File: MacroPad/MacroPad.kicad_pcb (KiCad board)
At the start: 2 copper layers, 75 x 118 mm, 35 parts, among them SW1 CherryMX, SW10 CherryMX, SW11 CherryMX, SW12 CherryMX, SW13 RotaryEncoder_Switch, SW14 SW_Push, SW15 SW_Push, SW16 SW_Push, SW2 CherryMX, SW3 CherryMX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

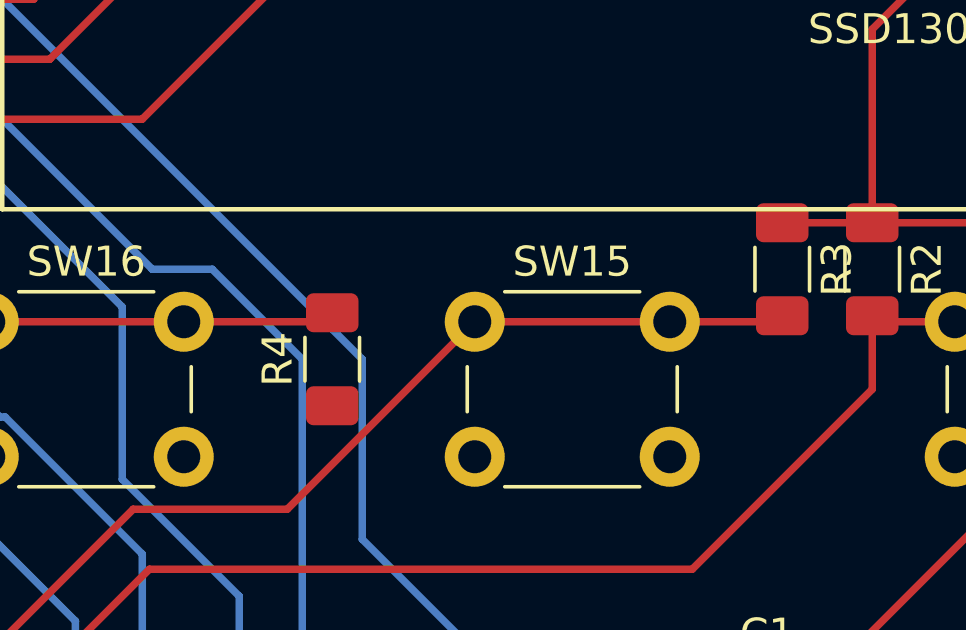
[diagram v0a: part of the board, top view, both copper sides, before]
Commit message: fixed position of R4 and GND connection
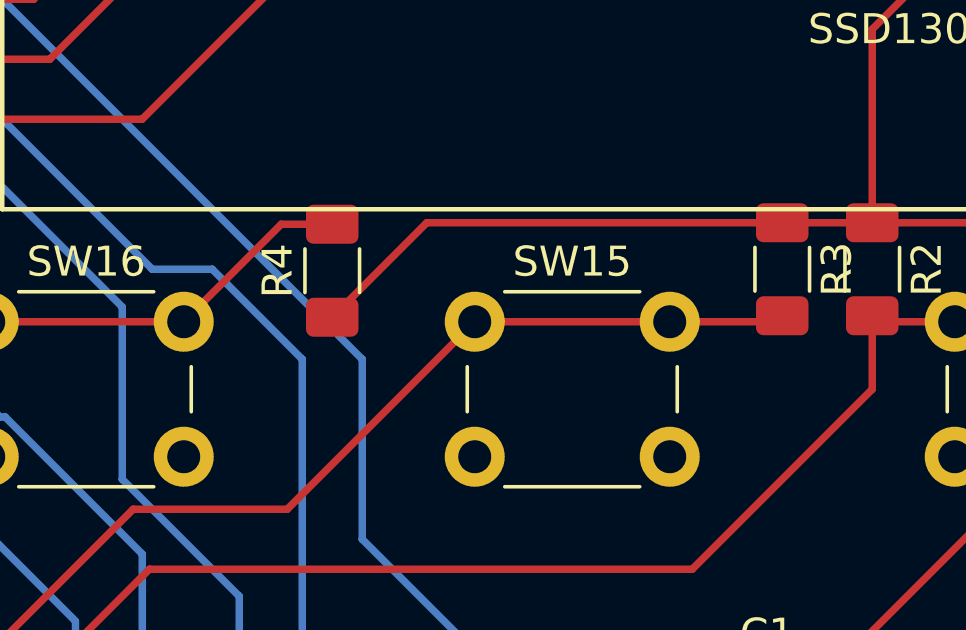
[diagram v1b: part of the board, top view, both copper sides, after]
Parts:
- moved R4 2.95 mm to (146.0, 85.0)
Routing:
- net GND: track 212.3 -> 228.6 mm
- net Button3: track 24.9 -> 26.2 mm
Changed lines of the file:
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@@
   )
   (footprint "Resistor_SMD:R_1206_3216Metric_Pad1.30x1.75mm_HandSolder" (layer "F.Cu")
-    (at 146 88 90)
+    (at 146 85.05 90)
     (descr "Resistor SMD 1206 (3216 Metric), square (rectangular) end terminal, IPC_7351 nominal with elongated pad for handsoldering. (Body size source: IPC-SM-782 page 72, https://www.pcb-3d.com/wordpress/wp-content/uploads/ipc-sm-782a_amendment_1_and_2.pdf), generated with kicad-footprint-generator")
     (tags "resistor handsolder")
@@
   (segment (start 117.55 174.4) (end 117.55 169.591919) (width 0.25) (layer "F.Cu") (net 2))
   (segment (start 146.42 165.42) (end 142.54 165.42) (width 0.25) (layer "F.Cu") (net 2))
+  (segment (start 149.15 83.45) (end 161 83.45) (width 0.25) (layer "F.Cu") (net 2))
   (segment (start 151.02 153.9) (end 142.54 145.42) (width 0.25) (layer "F.Cu") (net 2))
   (segment (start 137.55 109.591919) (end 141.721919 105.42) (width 0.25) (layer "F.Cu") (net 2))
@@
   (segment (start 162.0625 99) (end 162.54 99.4775) (width 0.25) (layer "F.Cu") (net 2))
   (segment (start 137.55 174.4) (end 137.55 169.591919) (width 0.25) (layer "F.Cu") (net 2))
+  (segment (start 146 86.6) (end 149.15 83.45) (width 0.25) (layer "F.Cu") (net 2))
   (segment (start 161 83.45) (end 164 83.45) (width 0.25) (layer "F.Cu") (net 2))
   (segment (start 137.55 129.591919) (end 141.721919 125.42) (width 0.25) (layer "F.Cu") (net 2))
@@
   (segment (start 161 86.55) (end 160.8 86.75) (width 0.25) (layer "F.Cu") (net 49))
   (segment (start 150.75 86.75) (end 157.25 86.75) (width 0.25) (layer "F.Cu") (net 49))
-  (segment (start 146 86.45) (end 145.7 86.75) (width 0.25) (layer "F.Cu") (net 50))
+  (segment (start 144.3 83.5) (end 141.05 86.75) (width 0.25) (layer "F.Cu") (net 50))
   (segment (start 134.55 86.75) (end 141.05 86.75) (width 0.25) (layer "F.Cu") (net 50))
+  (segment (start 146 83.5) (end 144.3 83.5) (width 0.25) (layer "F.Cu") (net 50))
   (segment (start 131.12344 90.17656) (end 134.55 86.75) (width 0.25) (layer "F.Cu") (net 50))
   (segment (start 131.12344 98.7) (end 131.12344 90.17656) (width 0.25) (layer "F.Cu") (net 50))
-  (segment (start 145.7 86.75) (end 141.05 86.75) (width 0.25) (layer "F.Cu") (net 50))
   (zone (net 1) (net_name "Net-(C1-Pad1)") (layer "F.Cu") (hatch edge 0.508)
     (connect_pads (clearance 0.5))

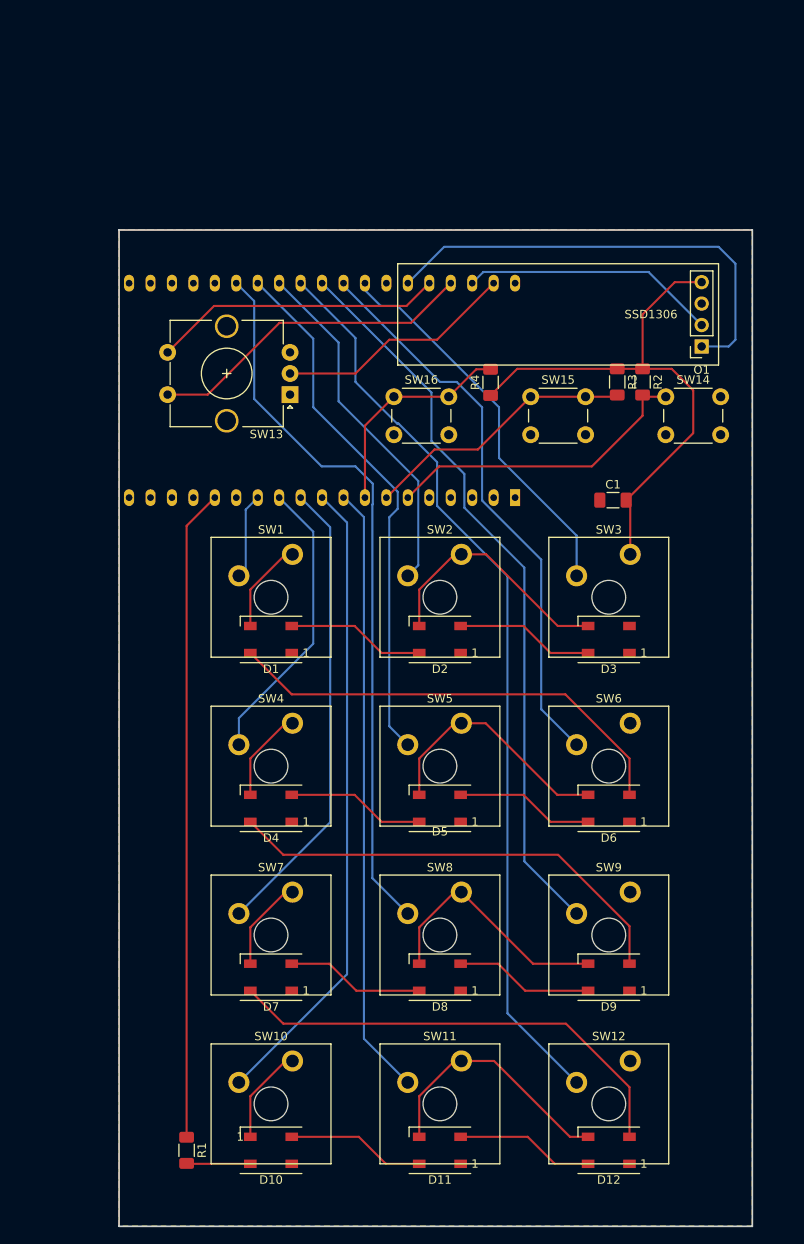
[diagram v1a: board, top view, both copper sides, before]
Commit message: updated PCB to devkitC V2
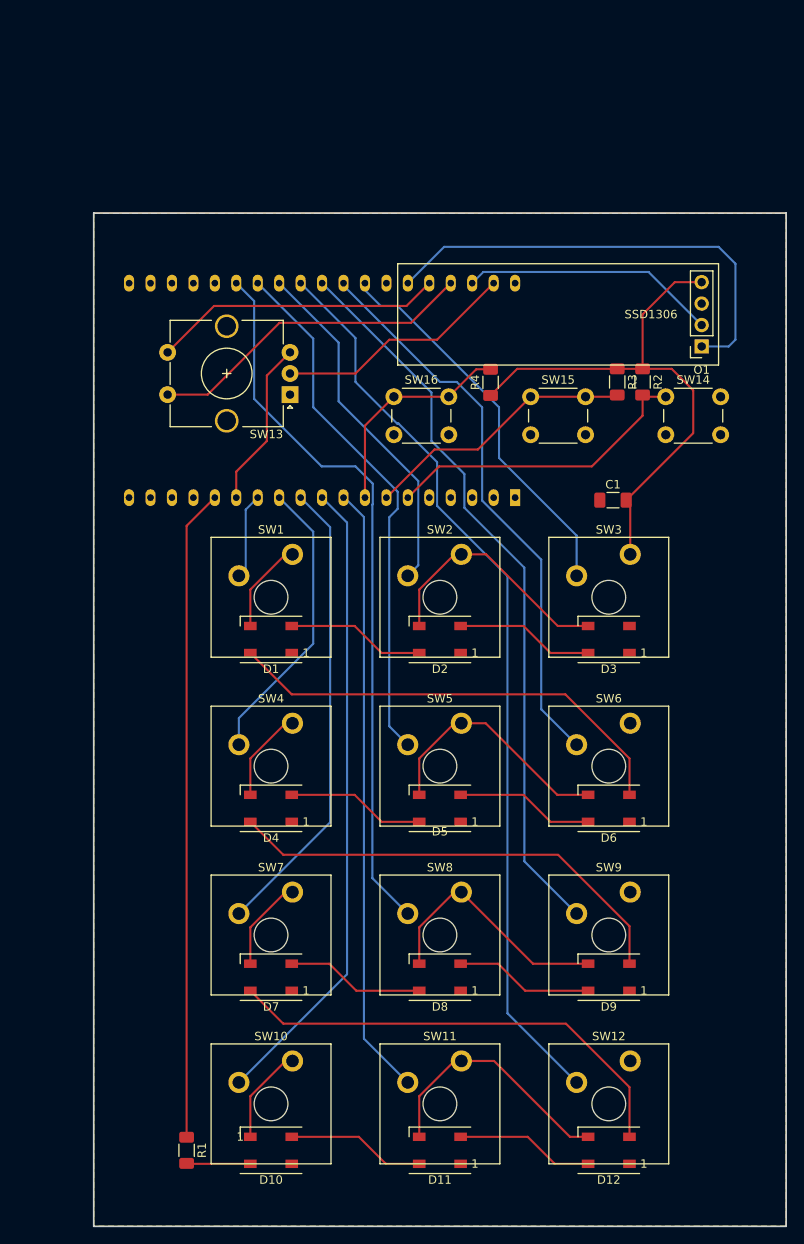
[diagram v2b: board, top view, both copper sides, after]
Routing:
- net GND: track 228.6 -> 248.5 mm
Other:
- board size 75 x 118 mm -> 82 x 120 mm
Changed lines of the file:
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@@
   (gr_line (start 135 83) (end 173 83) (layer "F.SilkS") (width 0.15))
   (gr_line (start 173 83) (end 173 71) (layer "F.SilkS") (width 0.15))
-  (gr_rect (start 102 67) (end 177 185) (layer "Edge.Cuts") (width 0.2) (fill none))
+  (gr_rect (start 99 65) (end 181 185) (layer "Edge.Cuts") (width 0.2) (fill none))
+  (segment (start 115.88344 95.61656) (end 115.88344 98.7) (width 0.25) (layer "F.Cu") (net 2))
   (segment (start 117.55 153.9) (end 117.55 149.591919) (width 0.25) (layer "F.Cu") (net 2))
   (segment (start 141.721919 105.42) (end 142.54 105.42) (width 0.25) (layer "F.Cu") (net 2))
@@
   (segment (start 155.4 174.4) (end 146.42 165.42) (width 0.25) (layer "F.Cu") (net 2))
   (segment (start 145.42 125.42) (end 142.54 125.42) (width 0.25) (layer "F.Cu") (net 2))
+  (segment (start 119.5 92) (end 115.88344 95.61656) (width 0.25) (layer "F.Cu") (net 2))
   (segment (start 117.55 174.4) (end 117.55 169.591919) (width 0.25) (layer "F.Cu") (net 2))
   (segment (start 146.42 165.42) (end 142.54 165.42) (width 0.25) (layer "F.Cu") (net 2))
@@
   (segment (start 121.721919 125.42) (end 122.54 125.42) (width 0.25) (layer "F.Cu") (net 2))
   (segment (start 117.55 133.9) (end 117.55 129.591919) (width 0.25) (layer "F.Cu") (net 2))
+  (segment (start 119.5 84.25) (end 119.5 92) (width 0.25) (layer "F.Cu") (net 2))
   (segment (start 157.55 174.4) (end 155.4 174.4) (width 0.25) (layer "F.Cu") (net 2))
   (segment (start 162.54 99.4775) (end 162.54 105.42) (width 0.25) (layer "F.Cu") (net 2))
   (segment (start 117.55 109.591919) (end 117.55 113.9) (width 0.25) (layer "F.Cu") (net 2))
+  (segment (start 122.25 81.5) (end 119.5 84.25) (width 0.25) (layer "F.Cu") (net 2))
   (segment (start 153.9 133.9) (end 145.42 125.42) (width 0.25) (layer "F.Cu") (net 2))
   (segment (start 171 73.18) (end 167.82 73.18) (width 0.25) (layer "F.Cu") (net 2))
@@
     (polygon
       (pts
-        (xy 177 185)
-        (xy 102 185)
-        (xy 102 67)
-        (xy 177 67)
+        (xy 181 185)
+        (xy 99 185)
+        (xy 99 65)
+        (xy 181 65)
       )
     )
@@
     (polygon
       (pts
-        (xy 177 185)
-        (xy 102 185)
-        (xy 102 67)
-        (xy 177 67)
+        (xy 181 185)
+        (xy 99 185)
+        (xy 99 65)
+        (xy 181 65)
       )
     )

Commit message: Plotted and Generated Drill and SVG files
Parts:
- added REF**: MountingHole_2.2mm_M2, MountingHole:MountingHole_2.2mm_M2, F.Cu at (94.0, 46.0)
- added REF**: MountingHole_2.2mm_M2, MountingHole:MountingHole_2.2mm_M2, F.Cu at (94.0, 158.0)
- added REF**: MountingHole_2.2mm_M2, MountingHole:MountingHole_2.2mm_M2, F.Cu at (168.0, 158.0)
- added REF**: MountingHole_2.2mm_M2, MountingHole:MountingHole_2.2mm_M2, F.Cu at (168.0, 46.0)
- moved SW16 24.7 mm to (125.5, 63.8)
- moved C1 24.7 mm to (151.5, 76.0)
- moved D1 24.7 mm to (111.0, 92.5)
- moved D10 24.7 mm to (111.0, 153.0)
- moved D11 24.7 mm to (131.0, 153.0)
- moved D12 24.7 mm to (151.0, 153.0)
- moved D2 24.7 mm to (131.0, 92.5)
- moved D3 24.7 mm to (151.0, 92.5)
- moved D4 24.7 mm to (111.0, 112.5)
- moved D5 24.7 mm to (131.0, 112.5)
- moved D6 24.7 mm to (151.0, 112.5)
- moved D7 24.7 mm to (111.0, 132.5)
- moved D8 24.7 mm to (131.0, 132.5)
- moved D9 24.7 mm to (151.0, 132.5)
- moved O1 24.7 mm to (162.0, 57.8)
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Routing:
- net GND: track 248.5 -> 306.1 mm
- net Net-(O1-Pad1): track 54.7 -> 53.2 mm
- net Net-(D1-Pad4): track 54.4 -> 55.5 mm
- net Net-(D4-Pad4): track 54.5 -> 55.5 mm

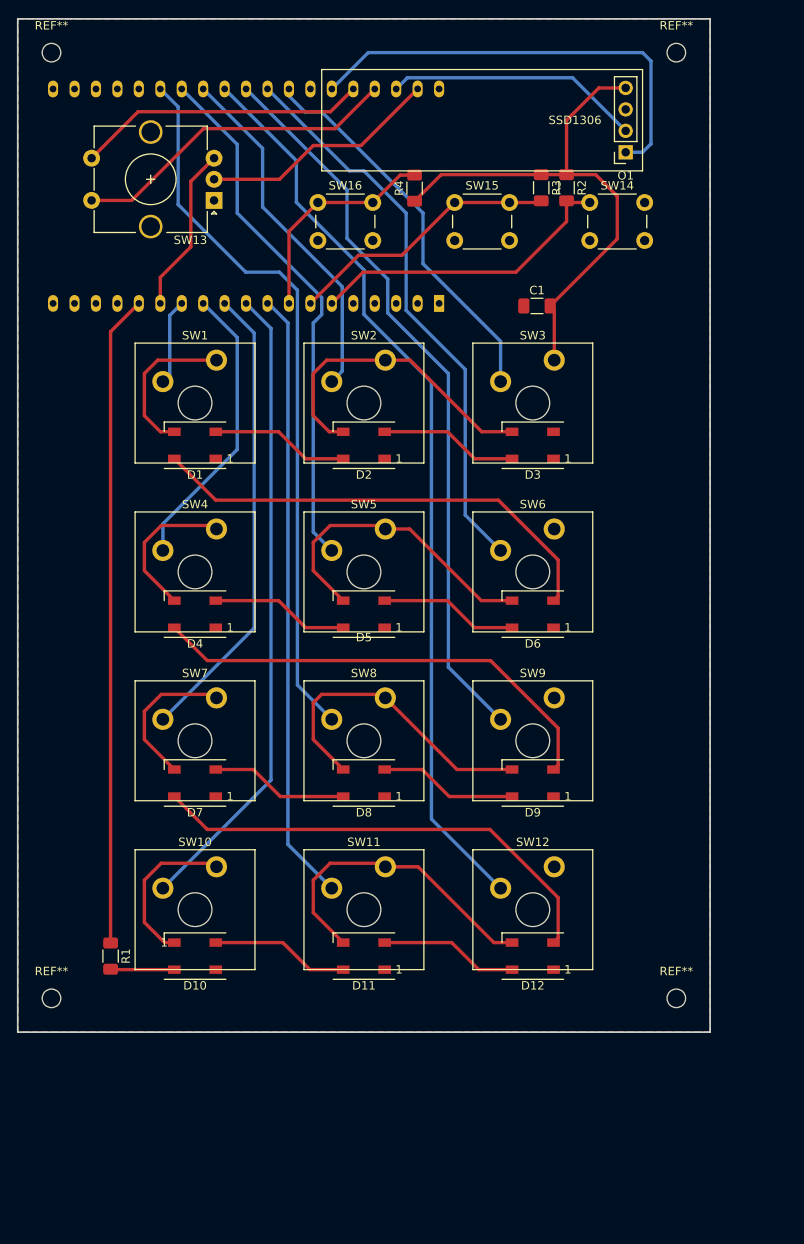
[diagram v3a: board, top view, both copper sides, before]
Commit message: Updated Silkscreen
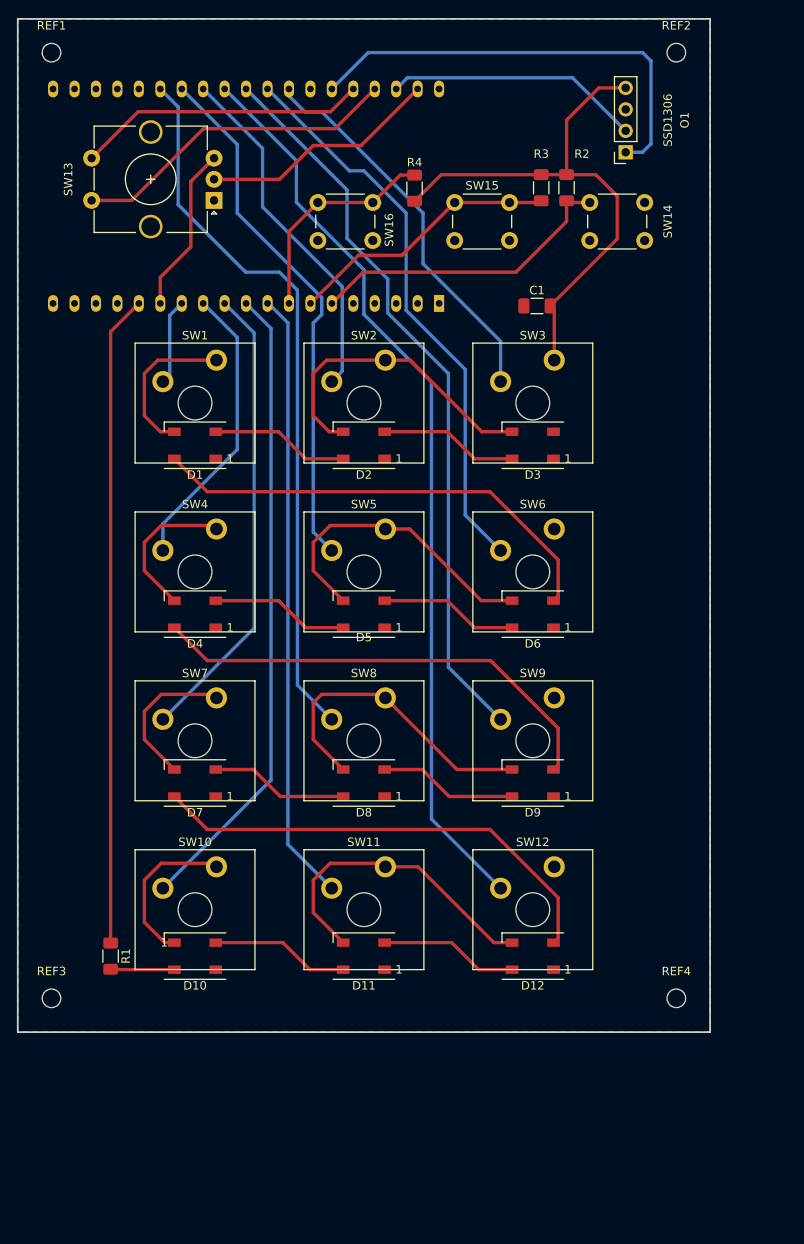
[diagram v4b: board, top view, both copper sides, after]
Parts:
- renumbered REF** to REF1, REF** to REF2, REF** to REF3, REF** to REF4
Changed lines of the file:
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@@
     (pad_to_mask_clearance 0)
     (pcbplotparams
-      (layerselection 0x00010fc_ffffffff)
+      (layerselection 0x00010fc_fffffffe)
       (disableapertmacros false)
       (usegerberextensions false)
       (usegerberattributes true)
       (usegerberadvancedattributes true)
-      (creategerberjobfile true)
+      (creategerberjobfile false)
       (svguseinch false)
       (svgprecision 6)
@@
       (sketchpadsonfab false)
       (subtractmaskfromsilk false)
-      (outputformat 1)
-      (mirror false)
+      (outputformat 4)
+      (mirror true)
       (drillshape 0)
       (scaleselection 1)
@@
     (tags "mounting hole 2.2mm no annular m2")
     (attr exclude_from_pos_files exclude_from_bom)
-    (fp_text reference "REF**" (at 0 -3.2) (layer "F.SilkS")
+    (fp_text reference "REF1" (at 0 -3.2) (layer "F.SilkS")
       (effects (font (size 1 1) (thickness 0.15)))
     )
@@
     (tags "mounting hole 2.2mm no annular m2")
     (attr exclude_from_pos_files exclude_from_bom)
-    (fp_text reference "REF**" (at 0 -3.2) (layer "F.SilkS")
+    (fp_text reference "REF3" (at 0 -3.2) (layer "F.SilkS")
       (effects (font (size 1 1) (thickness 0.15)))
     )
@@
     (property "Sheetname" "")
     (attr smd)
-    (fp_text reference "R2" (at 0 -1.82 90) (layer "F.SilkS")
+    (fp_text reference "R2" (at -4 -1.82 180) (layer "F.SilkS")
       (effects (font (size 1 1) (thickness 0.15)))
     )
@@
     (tags "mounting hole 2.2mm no annular m2")
     (attr exclude_from_pos_files exclude_from_bom)
-    (fp_text reference "REF**" (at 0 -3.2) (layer "F.SilkS")
+    (fp_text reference "REF4" (at 0 -3.2) (layer "F.SilkS")
       (effects (font (size 1 1) (thickness 0.15)))
     )
@@
     (tags "mounting hole 2.2mm no annular m2")
     (attr exclude_from_pos_files exclude_from_bom)
-    (fp_text reference "REF**" (at 0 -3.2) (layer "F.SilkS")
+    (fp_text reference "REF2" (at 0 -3.2) (layer "F.SilkS")
       (effects (font (size 1 1) (thickness 0.15)))
     )
@@
     (property "Sheetname" "")
     (attr through_hole)
-    (fp_text reference "SW14" (at 3.25 -2) (layer "F.SilkS")
+    (fp_text reference "SW14" (at 9.25 2.25 90) (layer "F.SilkS")
       (effects (font (size 1 1) (thickness 0.15)))
     )
@@
     (property "Sheetname" "")
     (attr through_hole)
-    (fp_text reference "SW16" (at 3.25 -2) (layer "F.SilkS")
+    (fp_text reference "SW16" (at 8.45 3.25 90) (layer "F.SilkS")
       (effects (font (size 1 1) (thickness 0.15)))
     )
@@
     (property "Sheetname" "")
     (attr smd)
-    (fp_text reference "R4" (at 0 -1.82 90) (layer "F.SilkS")
+    (fp_text reference "R4" (at 3.05 0 180) (layer "F.SilkS")
       (effects (font (size 1 1) (thickness 0.15)))
     )
@@
     (property "Sheetname" "")
     (attr through_hole)
-    (fp_text reference "SW13" (at 2.8 -4.7) (layer "F.SilkS")
+    (fp_text reference "SW13" (at 17.25 2.5 90) (layer "F.SilkS")
       (effects (font (size 1 1) (thickness 0.15)))
     )
@@
     (property "Sheetname" "")
     (attr through_hole)
-    (fp_text reference "O1" (at 0 -2.77 180) (layer "F.SilkS")
-      (effects (font (size 1 1) (thickness 0.15)))
-    )
-    (fp_text value "SSD1306" (at 6 3.8 180) (layer "F.SilkS")
+    (fp_text reference "O1" (at -7 3.8 270) (layer "F.SilkS")
+      (effects (font (size 1 1) (thickness 0.15)))
+    )
+    (fp_text value "SSD1306" (at -5 3.8 270) (layer "F.SilkS")
       (effects (font (size 1 1) (thickness 0.15)))
     )
@@
     (property "Sheetname" "")
     (attr smd)
-    (fp_text reference "R3" (at 0 -1.82 90) (layer "F.SilkS")
+    (fp_text reference "R3" (at -4 0 180) (layer "F.SilkS")
       (effects (font (size 1 1) (thickness 0.15)))
     )
@@
       (net 2 "GND") (pinfunction "GND") (pintype "power_in"))
   )
-  (gr_line (start 126 48) (end 126 60) (layer "F.SilkS") (width 0.15))
-  (gr_line (start 164 48) (end 126 48) (layer "F.SilkS") (width 0.15))
-  (gr_line (start 126 60) (end 164 60) (layer "F.SilkS") (width 0.15))
-  (gr_line (start 164 60) (end 164 48) (layer "F.SilkS") (width 0.15))
   (gr_rect (start 90 42) (end 172 162) (layer "Edge.Cuts") (width 0.2) (fill none))
   (segment (start 106.88344 72.61656) (end 106.88344 75.7) (width 0.4) (layer "F.Cu") (net 2))
@@
   (segment (start 120.9 90.9) (end 124.1 94.1) (width 0.4) (layer "F.Cu") (net 3))
   (segment (start 124.1 94.1) (end 128.55 94.1) (width 0.4) (layer "F.Cu") (net 3))
-  (segment (start 154 106.07096) (end 146.92904 99) (width 0.4) (layer "F.Cu") (net 4))
-  (segment (start 146.92904 99) (end 113.45 99) (width 0.4) (layer "F.Cu") (net 4))
+  (segment (start 154 110.35) (end 154 106.07096) (width 0.4) (layer "F.Cu") (net 4))
+  (segment (start 112.45 98) (end 108.55 94.1) (width 0.4) (layer "F.Cu") (net 4))
   (segment (start 153.45 110.9) (end 154 110.35) (width 0.4) (layer "F.Cu") (net 4))
-  (segment (start 154 110.35) (end 154 106.07096) (width 0.4) (layer "F.Cu") (net 4))
-  (segment (start 113.45 99) (end 108.55 94.1) (width 0.4) (layer "F.Cu") (net 4))
+  (segment (start 154 106.07096) (end 145.92904 98) (width 0.4) (layer "F.Cu") (net 4))
+  (segment (start 145.92904 98) (end 112.45 98) (width 0.4) (layer "F.Cu") (net 4))
   (segment (start 133.45 90.9) (end 140.9 90.9) (width 0.4) (layer "F.Cu") (net 5))
   (segment (start 144.1 94.1) (end 148.55 94.1) (width 0.4) (layer "F.Cu") (net 5))

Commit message: minor updates
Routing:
- net Button1: track 37.1 -> 43.6 mm
- net Net-(O1-Pad2): track 30.3 -> 31.1 mm
